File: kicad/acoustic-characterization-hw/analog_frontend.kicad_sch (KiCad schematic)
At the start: 1 part, among them U3 MS9280

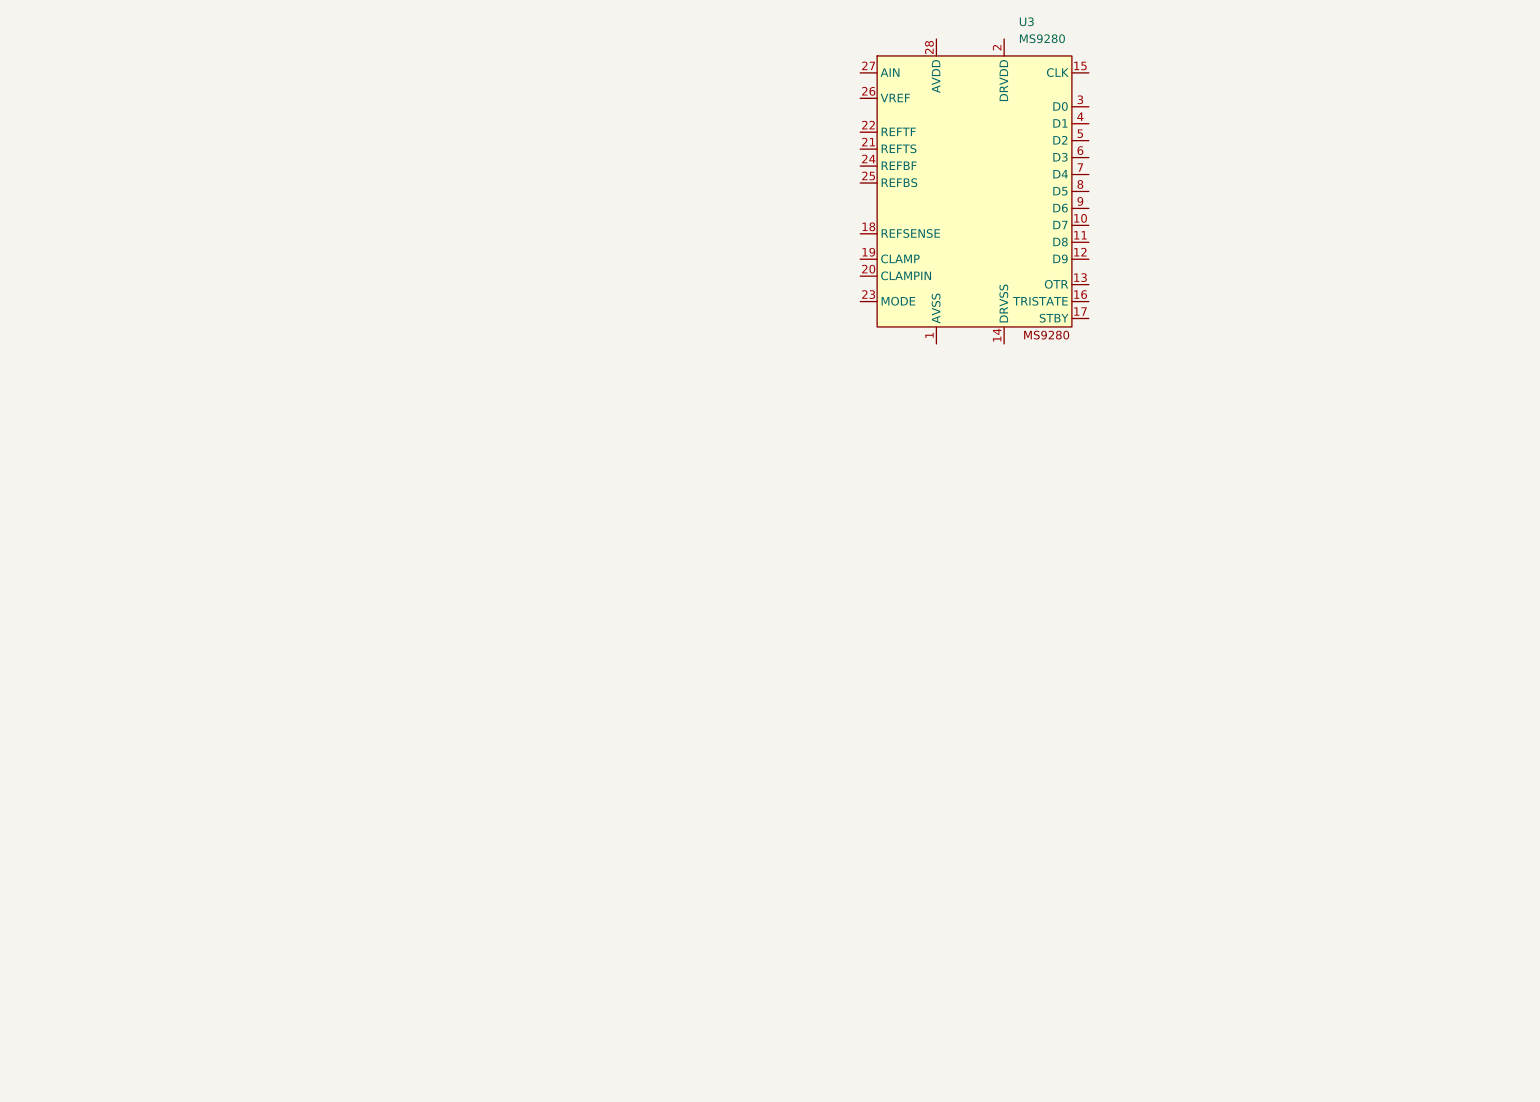
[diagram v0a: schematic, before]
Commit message: [kicad, documentation] Set pin configuration, kept possibility open for reference voltage change and top/bottom, center, differential mode
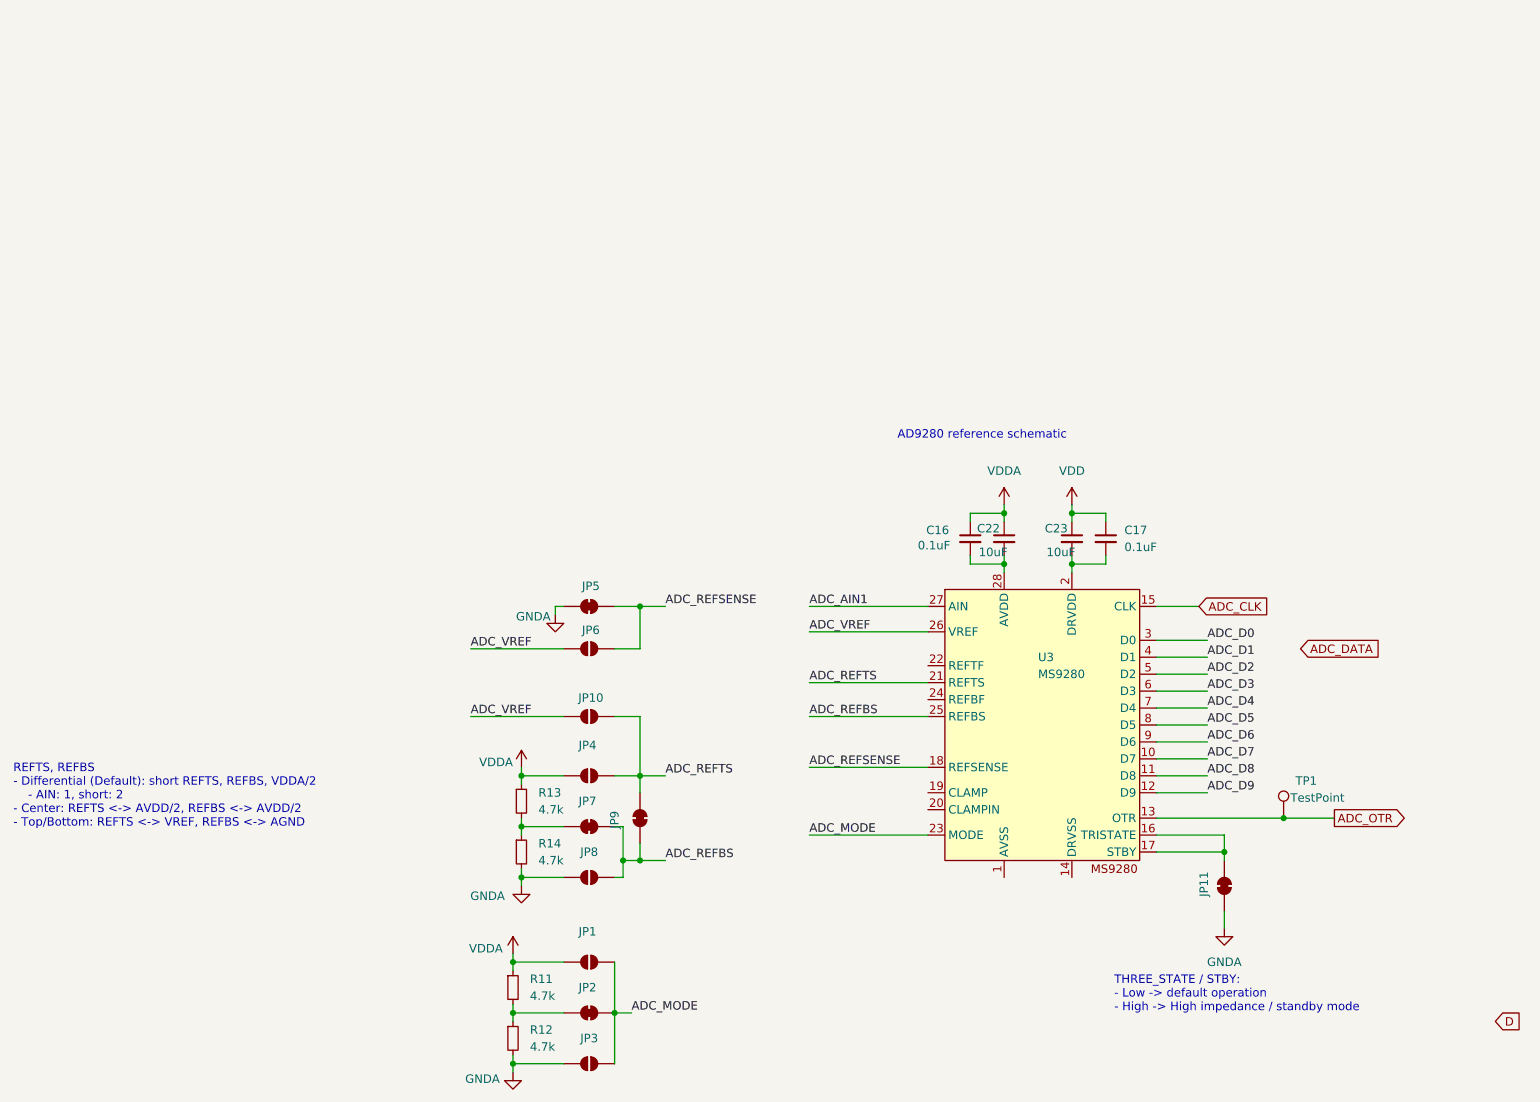
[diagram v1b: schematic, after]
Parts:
- added C16, C17: 0.1uF, Capacitor_SMD:C_0402_1005Metric, symbol Device:C_Small
- added C22, C23: 10uF, Capacitor_SMD:C_0603_1608Metric, symbol Device:C_Small
- added JP1, JP10, JP3, JP4, JP6, JP8: SolderJumper_2_Open, Jumper:SolderJumper-3_P1.3mm_Bridged12_Pad1.0x1.5mm_NumberLabels, symbol Jumper:SolderJumper_2_Open
- added JP11, JP2, JP5, JP7, JP9: SolderJumper_2_Bridged, symbol Jumper:SolderJumper_2_Bridged
- added R11, R12, R13, R14: 4.7k, Resistor_SMD:R_0402_1005Metric, symbol Device:R_Small
- added TP1: TestPoint, symbol Connector:TestPoint
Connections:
- net ADC_D7: now reaches U3.10 (D7)
- net ADC_D8: now reaches U3.11 (D8)
- net ADC_D9: now reaches U3.12 (D9)
- net ADC_OTR: now reaches U3.13 (OTR)
- net ADC_OTR: now also TP1.1
- net ADC_CLK: now reaches U3.15 (CLK)
- net at U3.16 (TRISTATE): now also U3.17 (STBY), JP11.2 (B)
- net ADC_REFSENSE: now reaches U3.18 (REFSENSE)
- net ADC_REFSENSE: now also JP5.2 (B), JP6.2 (B)
- net at U3.2 (DRVDD): now also C17.2, C23.2
- net ADC_REFTS: now reaches U3.21 (REFTS)
- net ADC_REFTS: now also JP10.2 (B), JP4.2 (B), JP9.2 (B)
- net ADC_MODE: now reaches U3.23 (MODE)
- net ADC_MODE: now also JP1.2 (B), JP2.2 (B), JP3.2 (B)
- net ADC_REFBS: now reaches U3.25 (REFBS)
- net ADC_REFBS: now also JP7.2 (B), JP8.2 (B), JP9.1 (A)
- net ADC_VREF: now reaches U3.26 (VREF)
- net ADC_VREF: now also JP10.1 (A), JP6.1 (A)
- net ADC_AIN1: now reaches U3.27 (AIN)
- net at U3.28 (AVDD): now also C16.2, C22.2
- net ADC_D0: now reaches U3.3 (D0)
- net ADC_D1: now reaches U3.4 (D1)
- net ADC_D2: now reaches U3.5 (D2)
- net ADC_D3: now reaches U3.6 (D3)
- net ADC_D4: now reaches U3.7 (D4)
- net ADC_D5: now reaches U3.8 (D5)
- net ADC_D6: now reaches U3.9 (D6)
- new net: JP2.1 (A), R11.2, R12.1
- new net: JP7.1 (A), R13.2, R14.1
- new net GNDA: JP11.1 (A), JP3.1 (A), JP5.1 (A), JP8.1 (A), R12.2, R14.2
- new net VDD: C17.1, C23.1
- new net VDDA: C16.1, C22.1, JP1.1 (A), JP4.1 (A), R11.1, R13.1
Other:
- note added: "AD9280 reference schematic"
- note added: "REFTS, REFBS - Differential (Default): short REFTS, REFBS, VDDA/2 - AIN: 1, short: 2 - Center: REFTS <-> AVDD/2, REFBS <-> AVDD/2 - Top/Bottom: REFTS <-> VREF, REFBS <-> AGND"
- note added: "THREE_STATE / STBY: - Low -> default operation - High -> High impedance / standby mode"
- moved on the sheet: U3

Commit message: [documentation, kicad] Added decoupling capacitors + input circuitry for adc (next) Look for a decent connector
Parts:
- removed TP1: TestPoint, symbol Connector:TestPoint
- added C24, C26, C27, C29: 0.1uF, Capacitor_SMD:C_0402_1005Metric, symbol Device:C_Small
- added C25: 1uF, Capacitor_SMD:C_0805_2012Metric, symbol Device:C_Small
- added C28: 10uF, Capacitor_SMD:C_0603_1608Metric, symbol Device:C_Small
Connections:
- net ADC_VREF: now also C24.1, C25.1
- net GNDA: now also U3.1 (AVSS), U3.19 (CLAMP), U3.20 (CLAMPIN), C24.2, C25.2, C26.2, C27.2
- net GND: now reaches U3.14 (DRVSS)
- net ADC_REFTF: now reaches U3.22 (REFTF)
- net ADC_REFTF: now also C27.1, C28.1, C29.1
- net ADC_REFBF: now reaches U3.24 (REFBF)
- net ADC_REFBF: now also C26.1, C28.2, C29.2
